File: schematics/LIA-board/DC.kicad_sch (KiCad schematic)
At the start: 33 parts, among them U1 LT8610, U2 LT3483AxS6, U3 LT3094xMSE, U4 ADP7118ACPZN, U5 ADP7118ACPZN

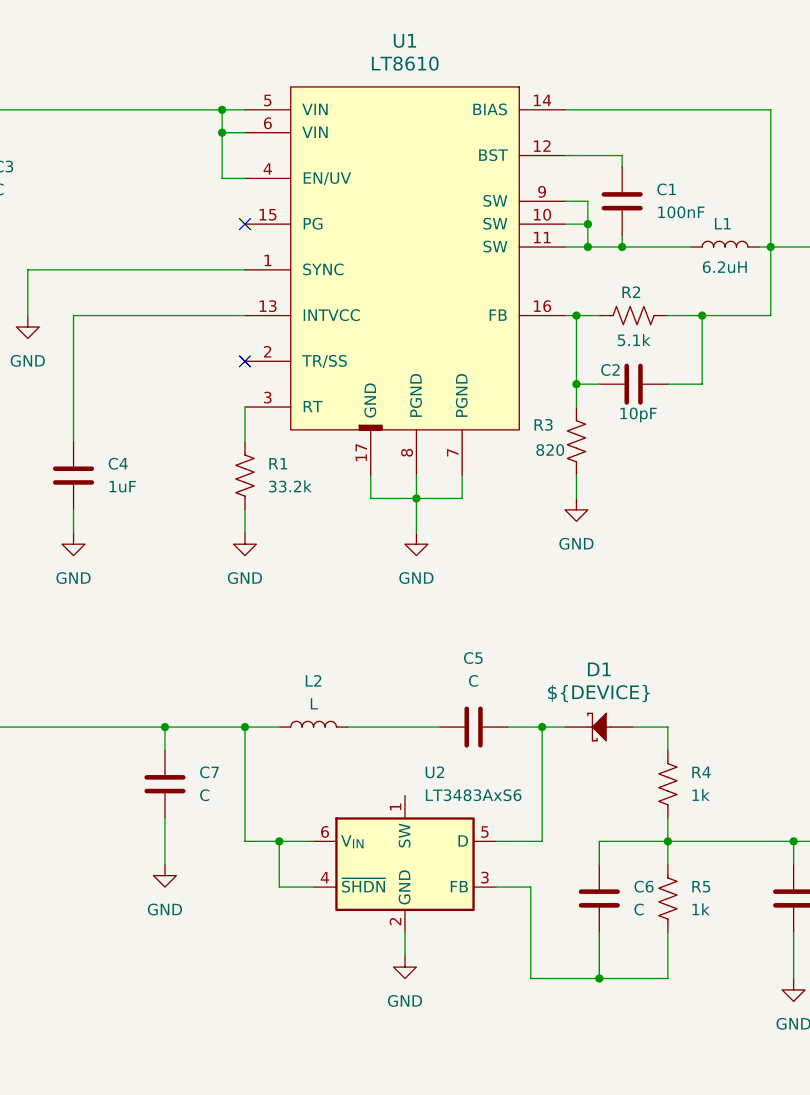
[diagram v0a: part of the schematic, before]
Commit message: some simulations, new page in kicad scematic
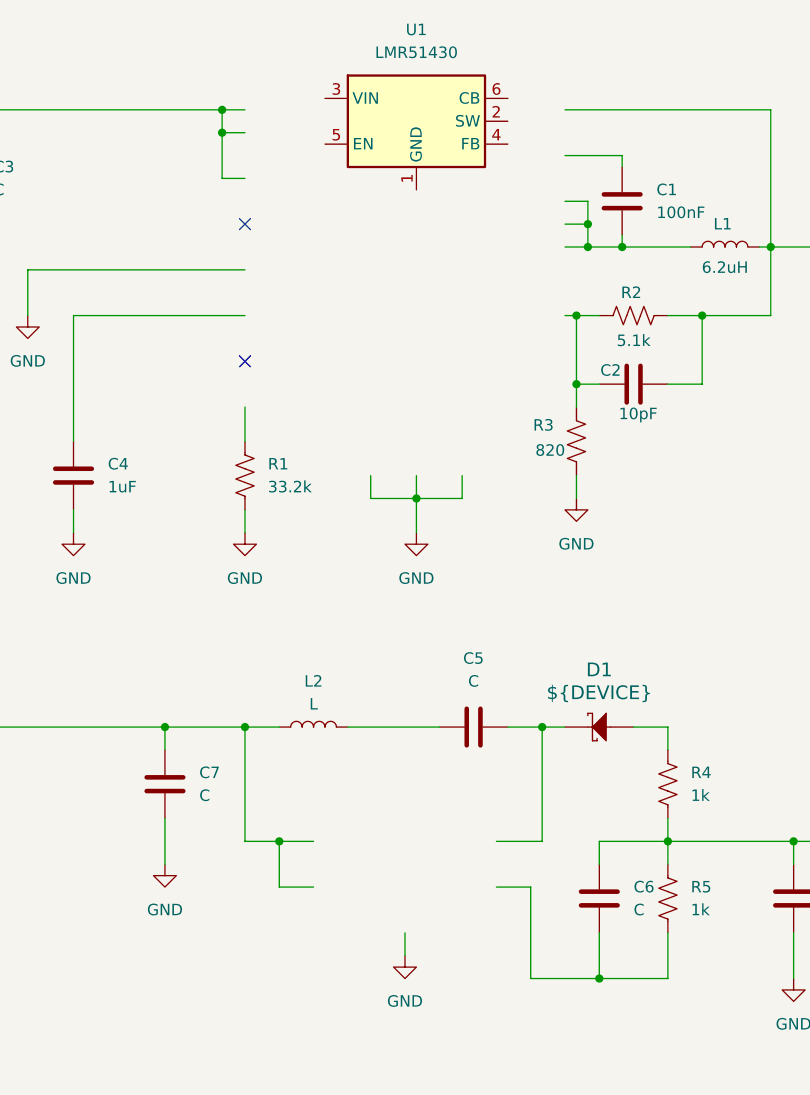
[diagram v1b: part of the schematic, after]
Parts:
- removed U1: LT8610, symbol CERN:LT8610
- removed U2: LT3483AxS6, Package_TO_SOT_SMD:TSOT-23-6, symbol Regulator_Switching:LT3483AxS6
- added U1: LMR51430, Package_TO_SOT_SMD:SOT-23-6, symbol Regulator_Switching:LMR51430
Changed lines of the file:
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@@
+	)
+	(symbol
+		(lib_id "Regulator_Switching:LMR51430")
+		(at 87.63 48.26 0)
+		(unit 1)
+		(body_style 1)
+		(exclude_from_sim no)
+		(in_bom yes)
+		(on_board yes)
+		(in_pos_files yes)
+		(dnp no)
+		(fields_autoplaced yes)
+		(property "Reference" "U1"
+			(at 87.63 38.1 0)
+			(show_name no)
+			(do_not_autoplace no)
+			(effects
+				(font
+					(size 1.27 1.27)
+				)
+			)
+		)
+		(property "Value" "LMR51430"
+			(at 87.63 40.64 0)
+			(show_name no)
+			(do_not_autoplace no)
+			(effects
+				(font
+					(size 1.27 1.27)
+				)
+			)
+		)
+		(property "Footprint" "Package_TO_SOT_SMD:SOT-23-6"
+			(at 88.9 57.15 0)
+			(hide yes)
+			(show_name no)
+			(do_not_autoplace no)
+			(effects
+				(font
+					(size 1.27 1.27)
+				)
+				(justify left)
+			)
+		)
+		(property "Datasheet" "https://www.ti.com/lit/ds/symlink/lmr51430.pdf"
+			(at 88.9 59.69 0)
+			(hide yes)
+			(show_name no)
+			(do_not_autoplace no)
+			(effects
+				(font
+					(size 1.27 1.27)
+				)
+				(justify left)
+			)
+		)
+		(property "Description" "4.5-V to 36-V, 3-A synchronous buck converter with 40-µA IQ, SOT-23-6"
+			(at 87.63 48.26 0)
+			(hide yes)
+			(show_name no)
+			(do_not_autoplace no)
+			(effects
+				(font
+					(size 1.27 1.27)
+				)
+			)
+		)
+		(pin "1"
+		)
+		(pin "5"
+		)
+		(pin "6"
+		)
+		(pin "2"
+		)
+		(pin "3"
+		)
+		(pin "4"
+		)
+		(instances
+			(project "GMOS-LIA"
+				(path "/87b3d1ed-39bd-4cff-a405-e580c48ff0ef/94922131-7715-4c45-944b-0843ad001e6a"
+					(reference "U1")
+					(unit 1)
+				)
+			)
+		)
 	)
 	(symbol
@@
 	)
 	(symbol
-		(lib_id "CERN:LT8610")
-		(at 73.66 44.45 0)
-		(unit 1)
-		(body_style 1)
-		(exclude_from_sim no)
-		(in_bom yes)
-		(on_board yes)
-		(in_pos_files yes)
-		(dnp no)
-		(fields_autoplaced yes)
-		(property "Reference" "U1"
-			(at 86.36 39.37 0)
-			(show_name no)
-			(do_not_autoplace no)
-			(effects
-				(font
-					(size 1.524 1.524)
-				)
-			)
-		)
-		(property "Value" "LT8610"
-			(at 86.36 41.91 0)
-			(show_name no)
-			(do_not_autoplace no)
-			(effects
-				(font
-					(size 1.524 1.524)
-				)
-			)
-		)
-		(property "Footprint" ""
-			(at 73.66 44.45 0)
-			(hide yes)
-			(show_name no)
-			(do_not_autoplace no)
-			(effects
-				(font
-					(size 1.27 1.27)
-				)
-			)
-		)
-		(property "Datasheet" ""
-			(at 73.66 44.45 0)
-			(hide yes)
-			(show_name no)
-			(do_not_autoplace no)
-			(effects
-				(font
-					(size 1.27 1.27)
-				)
-			)
-		)
-		(property "Description" "42V, 2.5A Synchronous Step-Down Regulator with 2.5µA Quiescent Current"
-			(at 73.66 44.45 0)
-			(hide yes)
-			(show_name no)
-			(do_not_autoplace no)
-			(effects
-				(font
-					(size 1.27 1.27)
-				)
-			)
-		)
-		(pin "13"
-		)
-		(pin "10"
-		)
-		(pin "1"
-		)
-		(pin "2"
-		)
-		(pin "7"
-		)
-		(pin "14"
-		)
-		(pin "12"
-		)
-		(pin "5"
-		)
-		(pin "8"
-		)
-		(pin "3"
-		)
-		(pin "4"
-		)
-		(pin "9"
-		)
-		(pin "6"
-		)
-		(pin "15"
-		)
-		(pin "17"
-		)
-		(pin "16"
-		)
-		(pin "11"
-		)
-		(instances
-			(project "GMOS-LIA"
-				(path "/87b3d1ed-39bd-4cff-a405-e580c48ff0ef/94922131-7715-4c45-944b-0843ad001e6a"
-					(reference "U1")
-					(unit 1)
-				)
-			)
-		)
-	)
-	(symbol
 		(lib_id "Device:C")
 		(at 173.99 52.07 0)
@@
 					(unit 1)
 				)
-			)
-		)
-	)
-	(symbol
-		(lib_id "Regulator_Switching:LT3483AxS6")
-		(at 86.36 130.81 0)
-		(unit 1)
-		(body_style 1)
-		(exclude_from_sim no)
-		(in_bom yes)
-		(on_board yes)
-		(in_pos_files yes)
-		(dnp no)
-		(fields_autoplaced yes)
-		(property "Reference" "U2"
-			(at 88.5033 120.65 0)
-			(show_name no)
-			(do_not_autoplace no)
-			(effects
-				(font
-					(size 1.27 1.27)
-				)
-				(justify left)
-			)
-		)
-		(property "Value" "LT3483AxS6"
-			(at 88.5033 123.19 0)
-			(show_name no)
-			(do_not_autoplace no)
-			(effects
-				(font
-					(size 1.27 1.27)
-				)
-				(justify left)
-			)
-		)
-		(property "Footprint" "Package_TO_SOT_SMD:TSOT-23-6"
-			(at 67.31 137.16 0)
-			(hide yes)
-			(show_name no)
-			(do_not_autoplace no)
-			(effects
-				(font
-					(size 1.27 1.27)
-				)
-			)
-		)
-		(property "Datasheet" "https://www.analog.com/media/en/technical-documentation/data-sheets/3483fc.pdf"
-			(at 86.36 139.7 0)
-			(hide yes)
-			(show_name no)
-			(do_not_autoplace no)
-			(effects
-				(font
-					(size 1.27 1.27)
-				)
-			)
-		)
-		(property "Description" "Inverting Micropower DC/DC Converter with integrated schottky, 2.5V to 16V input, down to -38V output, 400mA, TSOT-23-6 package"
-			(at 86.36 130.81 0)
-			(hide yes)
-			(show_name no)
-			(do_not_autoplace no)
-			(effects
-				(font
-					(size 1.27 1.27)
-				)
-			)
-		)
-		(pin "6"
-		)
-		(pin "5"
-		)
-		(pin "4"
-		)
-		(pin "3"
-		)
-		(pin "2"
-		)
-		(pin "1"
-		)
-		(instances
-			(project "GMOS-LIA"
-				(path "/87b3d1ed-39bd-4cff-a405-e580c48ff0ef/94922131-7715-4c45-944b-0843ad001e6a"
-					(reference "U2")
-					(unit 1)
-				)

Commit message: modified some of the scenatics
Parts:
- removed D1: ${DEVICE}, Diode_THT:D_DO-35_SOD27_P7.62mm_Horizontal, symbol CERN:Diode Schottky
- removed R1: 33.2k, SparkFun-Resistor:R_0603_1608Metric, symbol SparkFun:R
- added U18: LMR51430, Package_TO_SOT_SMD:SOT-23-6, symbol Regulator_Switching:LMR51430
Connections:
- net GND: now also C6.1, L2.2, R4.1, U1.1 (GND), U18.1 (GND)
- net at C3.1, C7.1: now also U1.3 (VIN), U1.5 (EN), U18.3 (VIN), U18.5 (EN); no longer L2.1
- net at U1.2 (SW): now also C1.2, L1.1
- net at U1.4 (FB): now also C2.1, R2.2, R3.1
- net at U1.6 (CB): now also C1.1
- net at C5.1: now also U18.6 (CB); no longer L2.2
- net at C5.2: now also L2.1, U18.2 (SW)
- net at C10.1, C8.1, U3.1 (IN)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: now also R5.2; no longer C6.1, R4.2, R5.1
- net at C12.1, C14.1, C2.2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: now also C4.1
- net at C6.2: now also R4.2, R5.1, U18.4 (FB); no longer R5.2
- no-connect marks 7 -> 5
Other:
- moved on the sheet: C3, C4, C5, C7, C8, R4, R5, U1

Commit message: some changes to board
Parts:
- removed C1: 100nF, SparkFun-Resistor:R_0603_1608Metric, symbol Device:C
- removed C10, C11, C12, C14, C6, C7, C8, C9: C, SparkFun-Resistor:R_0603_1608Metric, symbol Device:C
- removed C13, C15: 2.2uF, SparkFun-Resistor:R_0603_1608Metric, symbol Device:C
- removed C2: 10pF, SparkFun-Resistor:R_0603_1608Metric, symbol Device:C
- removed C3, C5: C, symbol Device:C
- removed C4: 1uF, symbol Device:C
- removed L1: 6.2uH, symbol Device:L
- removed L2: L, symbol Device:L
- removed R10, R2: 5.1k, SparkFun-Resistor:R_0603_1608Metric, symbol SparkFun:R
- removed R11: 1.6k, SparkFun-Resistor:R_0603_1608Metric, symbol SparkFun:R
- removed R12: 8.2k, SparkFun-Resistor:R_0603_1608Metric, symbol SparkFun:R
- removed R13: 4.7k, SparkFun-Resistor:R_0603_1608Metric, symbol SparkFun:R
- removed R3: 820, SparkFun-Resistor:R_0603_1608Metric, symbol SparkFun:R
- removed R4, R5: 1k, SparkFun-Resistor:R_0603_1608Metric, symbol SparkFun:R
- removed R8: 50k, SparkFun-Resistor:R_0603_1608Metric, symbol SparkFun:R
- removed U1, U18: LMR51430, Package_TO_SOT_SMD:SOT-23-6, symbol Regulator_Switching:LMR51430
- removed U3: LT3094xMSE, Package_SO:MSOP-12-1EP_3x4.039mm_P0.65mm_EP1.651x2.845mm, symbol Regulator_Linear:LT3094xMSE
- removed U4, U5: ADP7118ACPZN, Package_CSP:LFCSP-6-1EP_2x2mm_P0.65mm_EP1x1.6mm, symbol Regulator_Linear:ADP7118ACPZN
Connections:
- no-connect marks 5 -> 0
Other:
- added sheet Regulators (regulators.kicad_sch)
- added sheet USB_PD (usb_pd.kicad_sch)

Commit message: commit before changing LIA
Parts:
- added D4, D7: B5819W, symbol CERN:Diode Schottky
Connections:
- new net Regulators/Vin: D4.1 (C), D7.1 (C)
- new net USB_PD/V_USB_PD: D7.2 (A)
- new net Vin: D4.2 (A)
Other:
- sheet Regulators ports: added 3V3_iso, 5V_FTDI, FTDI_gnd, Vin; removed none
- sheet USB_PD ports: added V_USB_PD, i2c_scl, i2c_sda, usb_cc1, usb_cc2, usb_dp_rst, usb_pd_alert, usb_pd_attach; removed none

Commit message: changes to scematic
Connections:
- net Regulators/Vin renamed Regulators/VIN
- net Vin renamed VIN_LAB
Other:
- sheet Regulators: file regulators.kicad_sch -> REGULATORS.kicad_sch
- sheet Regulators ports: added VIN; removed Vin
- sheet USB_PD: file usb_pd.kicad_sch -> USB_PD.kicad_sch
- sheet USB_PD ports: added I2C_SCL, I2C_SDA, PD_ALERT; removed i2c_scl, i2c_sda, usb_pd_alert
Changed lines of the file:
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@@
 		)
 	)
-	(hierarchical_label "Vin"
+	(hierarchical_label "VIN_LAB"
 		(shape input)
 		(at 101.6 39.37 180)
@@
 		)
 	)
-	(hierarchical_label "i2c_sda"
+	(hierarchical_label "I2C_SDA"
 		(shape bidirectional)
 		(at 43.18 106.68 180)
@@
 		)
 	)
-	(hierarchical_label "i2c_scl"
+	(hierarchical_label "I2C_SCL"
 		(shape bidirectional)
 		(at 43.18 101.6 180)
@@
 			)
 		)
-		(property "Sheetfile" "regulators.kicad_sch"
+		(property "Sheetfile" "REGULATORS.kicad_sch"
 			(at 177.8 102.1846 0)
 			(show_name no)
@@
 			)
 		)
-		(pin "Vin" input
+		(pin "VIN" input
 			(at 177.8 73.66 180)
 			(effects
@@
 			)
 		)
-		(property "Sheetfile" "usb_pd.kicad_sch"
+		(property "Sheetfile" "USB_PD.kicad_sch"
 			(at 66.04 119.9646 0)
 			(show_name no)
@@
 			)
 		)
-		(pin "i2c_scl" tri_state
+		(pin "I2C_SCL" tri_state
 			(at 66.04 101.6 180)
 			(effects
@@
 			)
 		)
-		(pin "i2c_sda" tri_state
+		(pin "I2C_SDA" tri_state
 			(at 66.04 106.68 180)
 			(effects
@@
 			)
 		)
-		(pin "usb_pd_alert" output
+		(pin "PD_ALERT" output
 			(at 101.6 101.6 0)
 			(effects
